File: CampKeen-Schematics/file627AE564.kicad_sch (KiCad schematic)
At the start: 25 parts, among them Q16 2N7000, Q17 2N7000, Q18 2N7000, Q19 2N7000, Q60 LTV-847

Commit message: working on input protection.
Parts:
- Q60: footprint DIP762W60P254L1984H450Q16N -> SamacSys_Parts:DIP762W60P254L1984H450Q16N
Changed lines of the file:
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@@
     (property "Reference" "Q60" (id 0) (at 158.75 64.389 0))
     (property "Value" "LTV-847" (id 1) (at 158.75 66.7004 0))
-    (property "Footprint" "DIP762W60P254L1984H450Q16N" (id 2) (at 176.53 68.58 0)
+    (property "Footprint" "SamacSys_Parts:DIP762W60P254L1984H450Q16N" (id 2) (at 176.53 68.58 0)
       (effects (font (size 1.27 1.27)) (justify left) hide)
     )

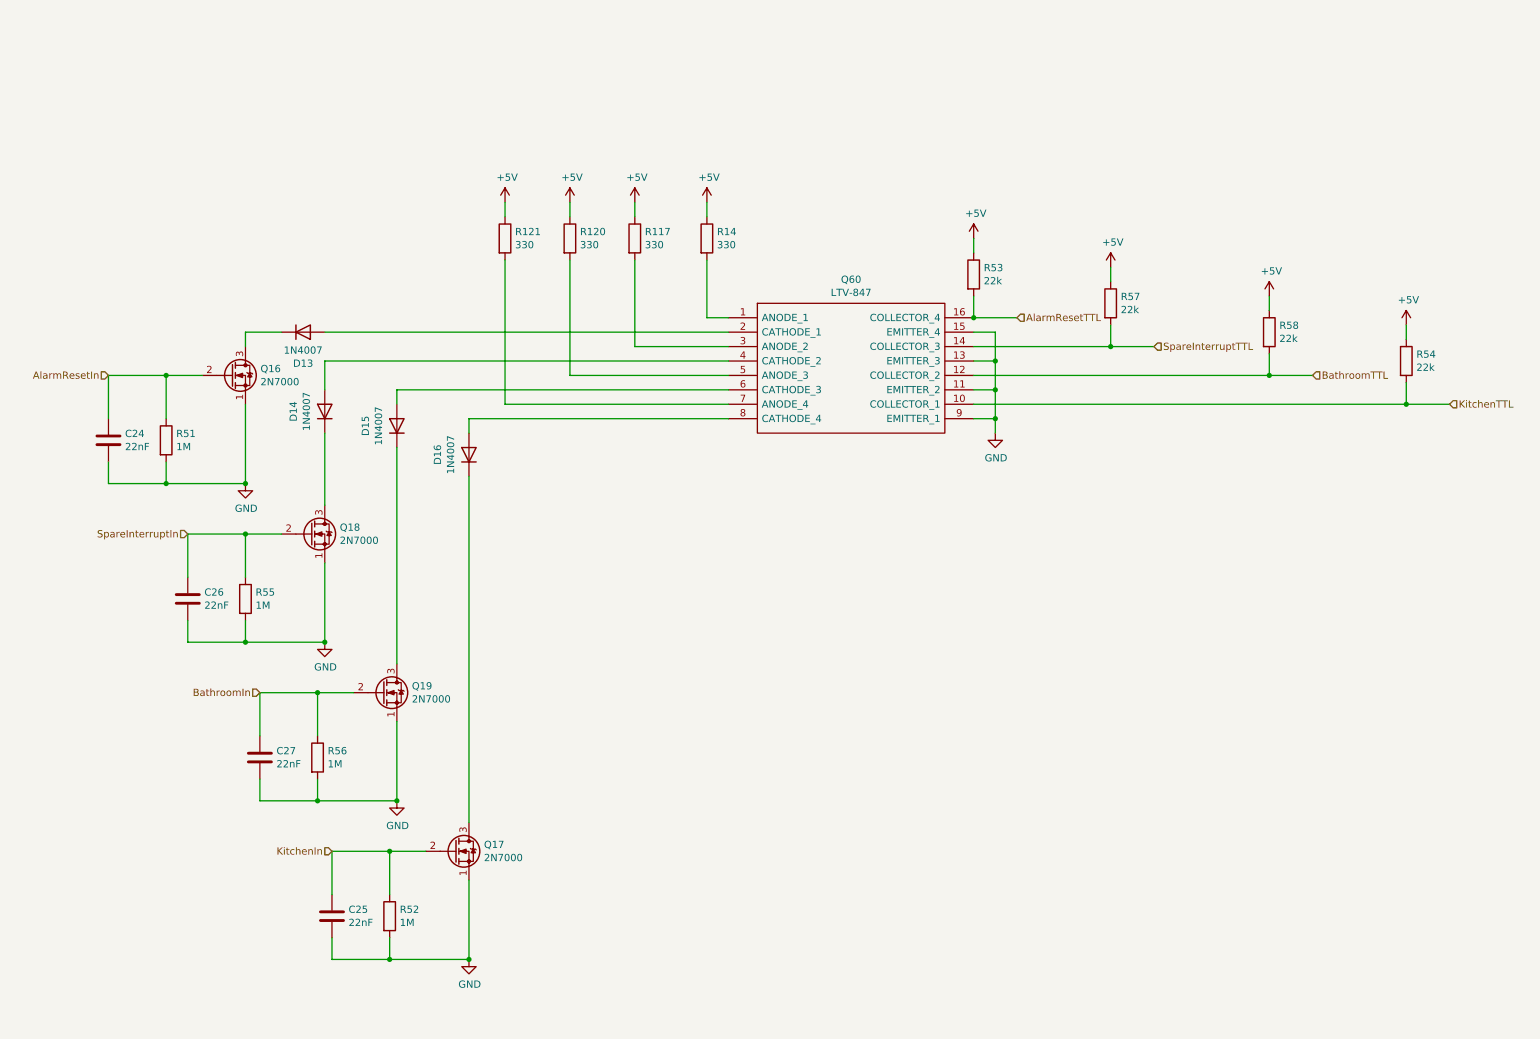
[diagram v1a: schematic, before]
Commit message: working on the input changes. removing all of the inverters. requires a code change. waiting on a part file to add the possible TVS diode
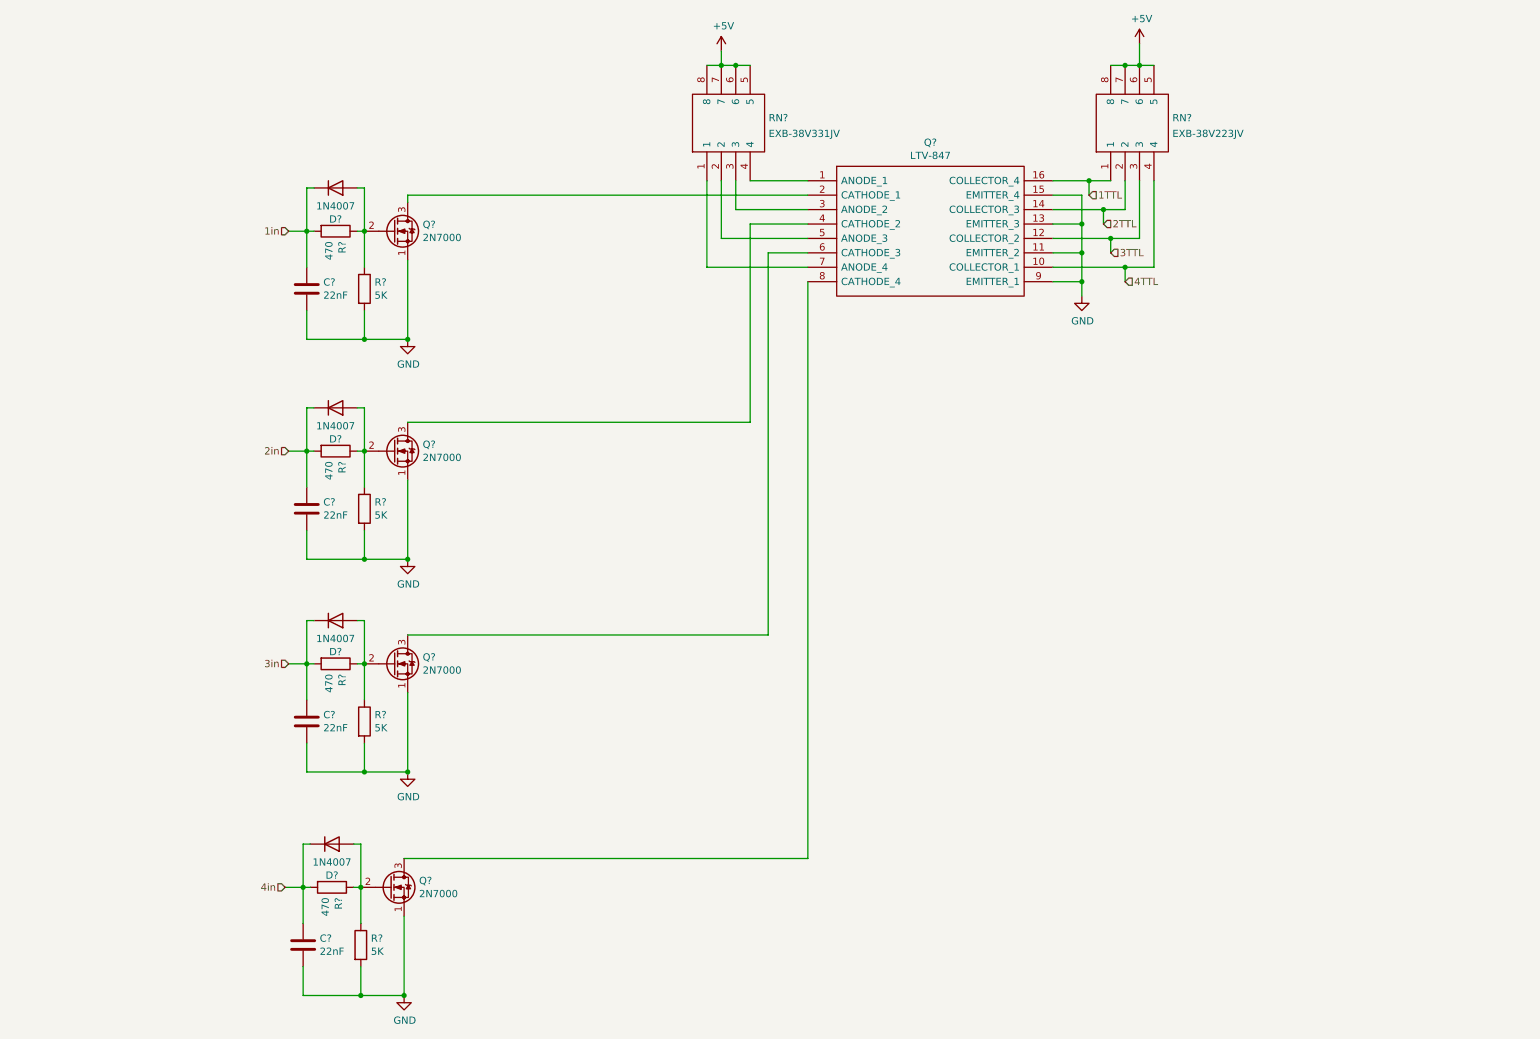
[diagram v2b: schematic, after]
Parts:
- removed C24, C25, C26, C27: 22nF, Capacitor_THT:C_Disc_D4.7mm_W2.5mm_P5.00mm, symbol Device:C
- removed D13, D14, D15, D16: 1N4007, Diode_THT:D_DO-41_SOD81_P10.16mm_Horizontal, symbol Diode:1N4007
- removed Q16, Q17, Q18, Q19: 2N7000, Package_TO_SOT_THT:TO-92_Inline, symbol Transistor_FET:2N7000
- removed Q60: LTV-847, SamacSys_Parts:DIP762W60P254L1984H450Q16N, symbol SamacSys_Parts:LTV-847
- removed R117, R120, R121, R14: 330, Resistor_THT:R_Axial_DIN0207_L6.3mm_D2.5mm_P2.54mm_Vertical, symbol Device:R
- removed R51, R52, R55, R56: 1M, Resistor_THT:R_Axial_DIN0207_L6.3mm_D2.5mm_P2.54mm_Vertical, symbol Device:R
- removed R53, R54, R57, R58: 22k, Resistor_THT:R_Axial_DIN0207_L6.3mm_D2.5mm_P2.54mm_Vertical, symbol Device:R
- added C? (x4): 22nF, Capacitor_SMD:C_0603_1608Metric_Pad1.08x0.95mm_HandSolder, symbol Device:C
- added D? (x4): 1N4007, Diode_THT:D_DO-41_SOD81_P10.16mm_Horizontal, symbol Diode:1N4007
- added Q? (x4): 2N7000, Package_TO_SOT_THT:TO-92_Inline, symbol Transistor_FET:2N7000
- added Q?: LTV-847, SamacSys_Parts:DIP762W60P254L1984H450Q16N, symbol SamacSys_Parts:LTV-847
- added R? (x4): 470, Resistor_THT:R_Axial_DIN0207_L6.3mm_D2.5mm_P2.54mm_Vertical, symbol Device:R
- added R? (x4): 5K, Resistor_THT:R_Axial_DIN0207_L6.3mm_D2.5mm_P2.54mm_Vertical, symbol Device:R
- added RN?: EXB-38V331JV, EXB38V472JV, symbol Samac_Sys:EXB-38V331JV
- added RN?: EXB-38V223JV, EXB38V472JV, symbol Samac_Sys:EXB-38V223JV
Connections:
- net +5V: now also RN?.5, RN?.5, RN?.6, RN?.6, RN?.7, RN?.7, RN?.8, RN?.8
- net GND: now also C?.2, C?.2, C?.2, C?.2, Q?.1 (S), Q?.1 (S), Q?.1 (S), Q?.1 (S), Q?.11 (EMITTER_2), Q?.13 (EMITTER_3), Q?.15 (EMITTER_4), Q?.9 (EMITTER_1), R?.2, R?.2, R?.2, R?.2
- new net: D?.2 (A), Q?.2 (G), R?.1, R?.1 (x4)
- new net: Q?.7 (ANODE_4), RN?.1
- new net: Q?.5 (ANODE_3), RN?.2
- new net: Q?.3 (ANODE_2), RN?.3
- new net: Q?.1 (ANODE_1), RN?.4
- new net: Q?.2 (CATHODE_1), Q?.3 (D)
- new net: Q?.3 (D), Q?.4 (CATHODE_2)
- new net: Q?.3 (D), Q?.6 (CATHODE_3)
- new net: Q?.3 (D), Q?.8 (CATHODE_4)
- new net 1TTL: Q?.16 (COLLECTOR_4), RN?.1
- new net 1in: C?.1, D?.1 (K), R?.2
- new net 2TTL: Q?.14 (COLLECTOR_3), RN?.2
- new net 2in: C?.1, D?.1 (K), R?.2
- new net 3TTL: Q?.12 (COLLECTOR_2), RN?.3
- new net 3in: C?.1, D?.1 (K), R?.2
- new net 4TTL: Q?.10 (COLLECTOR_1), RN?.4
- new net 4in: C?.1, D?.1 (K), R?.2

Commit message: wip
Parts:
- gave numbers to parts that had none: 23
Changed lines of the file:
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@@
   (symbol (lib_id "Device:R") (at 67.945 132.08 270)
     (in_bom yes) (on_board yes)
-    (property "Reference" "R?" (id 0) (at 69.1134 133.858 0)
+    (property "Reference" "R70" (id 0) (at 69.1134 133.858 0)
       (effects (font (size 1.27 1.27)) (justify left))
     )
@@
   (symbol (lib_id "Diode:1N4007") (at 67.945 86.995 0) (mirror x)
     (in_bom yes) (on_board yes)
-    (property "Reference" "D?" (id 0) (at 67.945 92.5068 0))
+    (property "Reference" "D22" (id 0) (at 67.945 92.5068 0))
     (property "Value" "1N4007" (id 1) (at 67.945 90.1954 0))
     (property "Footprint" "Diode_THT:D_DO-41_SOD81_P10.16mm_Horizontal" (id 2) (at 67.945 82.55 0)
@@
   (symbol (lib_id "power:+5V") (at 135.89 24.13 0)
     (in_bom yes) (on_board yes)
-    (property "Reference" "#PWR?" (id 0) (at 135.89 27.94 0)
+    (property "Reference" "#PWR0152" (id 0) (at 135.89 27.94 0)
       (effects (font (size 1.27 1.27)) hide)
     )
@@
   (symbol (lib_id "Samac_Sys:EXB-38V331JV") (at 133.35 46.99 90)
     (in_bom yes) (on_board yes) (fields_autoplaced)
-    (property "Reference" "RN?" (id 0) (at 144.2212 35.9215 90)
+    (property "Reference" "RN9" (id 0) (at 144.2212 35.9215 90)
       (effects (font (size 1.27 1.27)) (justify right))
     )
@@
   (symbol (lib_id "power:GND") (at 80.645 151.13 0)
     (in_bom yes) (on_board yes)
-    (property "Reference" "#PWR?" (id 0) (at 80.645 157.48 0)
+    (property "Reference" "#PWR0156" (id 0) (at 80.645 157.48 0)
       (effects (font (size 1.27 1.27)) hide)
     )
@@
   (symbol (lib_id "Transistor_FET:2N7000") (at 78.105 55.88 0)
     (in_bom yes) (on_board yes)
-    (property "Reference" "Q?" (id 0) (at 83.2866 54.7116 0)
+    (property "Reference" "Q27" (id 0) (at 83.2866 54.7116 0)
       (effects (font (size 1.27 1.27)) (justify left))
     )
@@
   (symbol (lib_id "Device:R") (at 67.945 55.88 270)
     (in_bom yes) (on_board yes)
-    (property "Reference" "R?" (id 0) (at 69.1134 57.658 0)
+    (property "Reference" "R68" (id 0) (at 69.1134 57.658 0)
       (effects (font (size 1.27 1.27)) (justify left))
     )
@@
   (symbol (lib_id "Diode:1N4007") (at 67.945 124.46 0) (mirror x)
     (in_bom yes) (on_board yes)
-    (property "Reference" "D?" (id 0) (at 67.945 129.9718 0))
+    (property "Reference" "D23" (id 0) (at 67.945 129.9718 0))
     (property "Value" "1N4007" (id 1) (at 67.945 127.6604 0))
     (property "Footprint" "Diode_THT:D_DO-41_SOD81_P10.16mm_Horizontal" (id 2) (at 67.945 120.015 0)
@@
   (symbol (lib_id "power:GND") (at 199.39 67.31 0)
     (in_bom yes) (on_board yes)
-    (property "Reference" "#PWR?" (id 0) (at 199.39 73.66 0)
+    (property "Reference" "#PWR0155" (id 0) (at 199.39 73.66 0)
       (effects (font (size 1.27 1.27)) hide)
     )
@@
   (symbol (lib_id "SamacSys_Parts:LTV-847") (at 151.13 46.99 0)
     (in_bom yes) (on_board yes)
-    (property "Reference" "Q?" (id 0) (at 172.72 40.259 0))
+    (property "Reference" "Q54" (id 0) (at 172.72 40.259 0))
     (property "Value" "LTV-847" (id 1) (at 172.72 42.5704 0))
     (property "Footprint" "SamacSys_Parts:DIP762W60P254L1984H450Q16N" (id 2) (at 190.5 44.45 0)
@@
   (symbol (lib_id "power:GND") (at 80.645 113.665 0)
     (in_bom yes) (on_board yes)
-    (property "Reference" "#PWR?" (id 0) (at 80.645 120.015 0)
+    (property "Reference" "#PWR0123" (id 0) (at 80.645 120.015 0)
       (effects (font (size 1.27 1.27)) hide)
     )
@@
   (symbol (lib_id "power:GND") (at 80.01 190.5 0)
     (in_bom yes) (on_board yes)
-    (property "Reference" "#PWR?" (id 0) (at 80.01 196.85 0)
+    (property "Reference" "#PWR0150" (id 0) (at 80.01 196.85 0)
       (effects (font (size 1.27 1.27)) hide)
     )
@@
   (symbol (lib_id "Device:R") (at 67.945 94.615 270)
     (in_bom yes) (on_board yes)
-    (property "Reference" "R?" (id 0) (at 69.1134 96.393 0)
+    (property "Reference" "R69" (id 0) (at 69.1134 96.393 0)
       (effects (font (size 1.27 1.27)) (justify left))
     )
@@
   (symbol (lib_id "Diode:1N4007") (at 67.31 163.83 0) (mirror x)
     (in_bom yes) (on_board yes)
-    (property "Reference" "D?" (id 0) (at 67.31 169.3418 0))
+    (property "Reference" "D20" (id 0) (at 67.31 169.3418 0))
     (property "Value" "1N4007" (id 1) (at 67.31 167.0304 0))
     (property "Footprint" "Diode_THT:D_DO-41_SOD81_P10.16mm_Horizontal" (id 2) (at 67.31 159.385 0)
@@
   (symbol (lib_id "Device:R") (at 67.31 171.45 270)
     (in_bom yes) (on_board yes)
-    (property "Reference" "R?" (id 0) (at 68.4784 173.228 0)
+    (property "Reference" "R67" (id 0) (at 68.4784 173.228 0)
       (effects (font (size 1.27 1.27)) (justify left))
     )
@@
   (symbol (lib_id "Device:R") (at 73.025 104.775 0)
     (in_bom yes) (on_board yes)
-    (property "Reference" "R?" (id 0) (at 74.803 103.6066 0)
+    (property "Reference" "R73" (id 0) (at 74.803 103.6066 0)
       (effects (font (size 1.27 1.27)) (justify left))
     )
@@
   (symbol (lib_id "Device:R") (at 73.025 142.24 0)
     (in_bom yes) (on_board yes)
-    (property "Reference" "R?" (id 0) (at 74.803 141.0716 0)
+    (property "Reference" "R74" (id 0) (at 74.803 141.0716 0)
       (effects (font (size 1.27 1.27)) (justify left))
     )
@@
   (symbol (lib_id "Transistor_FET:2N7000") (at 77.47 171.45 0)
     (in_bom yes) (on_board yes)
-    (property "Reference" "Q?" (id 0) (at 82.6516 170.2816 0)
+    (property "Reference" "Q26" (id 0) (at 82.6516 170.2816 0)
       (effects (font (size 1.27 1.27)) (justify left))
     )
@@
   (symbol (lib_id "Device:C") (at 62.865 66.04 0)
     (in_bom yes) (on_board yes)
-    (property "Reference" "C?" (id 0) (at 65.786 64.8716 0)
+    (property "Reference" "C38" (id 0) (at 65.786 64.8716 0)
       (effects (font (size 1.27 1.27)) (justify left))
     )
@@
   (symbol (lib_id "power:GND") (at 80.645 74.93 0)
     (in_bom yes) (on_board yes)
-    (property "Reference" "#PWR?" (id 0) (at 80.645 81.28 0)
+    (property "Reference" "#PWR0124" (id 0) (at 80.645 81.28 0)
       (effects (font (size 1.27 1.27)) hide)
     )
@@
   (symbol (lib_id "Device:R") (at 73.025 66.04 0)
     (in_bom yes) (on_board yes)
-    (property "Reference" "R?" (id 0) (at 74.803 64.8716 0)
+    (property "Reference" "R72" (id 0) (at 74.803 64.8716 0)
       (effects (font (size 1.27 1.27)) (justify left))
     )
@@
   (symbol (lib_id "Device:R") (at 72.39 181.61 0)
     (in_bom yes) (on_board yes)
-    (property "Reference" "R?" (id 0) (at 74.168 180.4416 0)
+    (property "Reference" "R71" (id 0) (at 74.168 180.4416 0)
       (effects (font (size 1.27 1.27)) (justify left))
     )
@@
   (symbol (lib_id "Transistor_FET:2N7000") (at 78.105 132.08 0)
     (in_bom yes) (on_board yes)
-    (property "Reference" "Q?" (id 0) (at 83.2866 130.9116 0)
+    (property "Reference" "Q29" (id 0) (at 83.2866 130.9116 0)
       (effects (font (size 1.27 1.27)) (justify left))
     )
@@
   (symbol (lib_id "Device:C") (at 62.865 104.775 0)
     (in_bom yes) (on_board yes)
-    (property "Reference" "C?" (id 0) (at 65.786 103.6066 0)
+    (property "Reference" "C39" (id 0) (at 65.786 103.6066 0)
       (effects (font (size 1.27 1.27)) (justify left))
     )
@@
   (symbol (lib_id "power:+5V") (at 209.55 22.86 0)
     (in_bom yes) (on_board yes)
-    (property "Reference" "#PWR?" (id 0) (at 209.55 26.67 0)
+    (property "Reference" "#PWR0153" (id 0) (at 209.55 26.67 0)
       (effects (font (size 1.27 1.27)) hide)
     )
@@
   (symbol (lib_id "Samac_Sys:EXB-38V223JV") (at 204.47 46.99 90)
     (in_bom yes) (on_board yes) (fields_autoplaced)
-    (property "Reference" "RN?" (id 0) (at 215.3412 35.9215 90)
+    (property "Reference" "RN10" (id 0) (at 215.3412 35.9215 90)
       (effects (font (size 1.27 1.27)) (justify right))
     )
@@
   (symbol (lib_id "Transistor_FET:2N7000") (at 78.105 94.615 0)
     (in_bom yes) (on_board yes)
-    (property "Reference" "Q?" (id 0) (at 83.2866 93.4466 0)
+    (property "Reference" "Q28" (id 0) (at 83.2866 93.4466 0)
       (effects (font (size 1.27 1.27)) (justify left))
     )
@@
   (symbol (lib_id "Device:C") (at 62.23 181.61 0)
     (in_bom yes) (on_board yes)
-    (property "Reference" "C?" (id 0) (at 65.151 180.4416 0)
+    (property "Reference" "C37" (id 0) (at 65.151 180.4416 0)
       (effects (font (size 1.27 1.27)) (justify left))
     )
@@
   (symbol (lib_id "Device:C") (at 62.865 142.24 0)
     (in_bom yes) (on_board yes)
-    (property "Reference" "C?" (id 0) (at 65.786 141.0716 0)
+    (property "Reference" "C40" (id 0) (at 65.786 141.0716 0)
       (effects (font (size 1.27 1.27)) (justify left))
     )
@@
   (symbol (lib_id "Diode:1N4007") (at 67.945 48.26 0) (mirror x)
     (in_bom yes) (on_board yes)
-    (property "Reference" "D?" (id 0) (at 67.945 53.7718 0))
+    (property "Reference" "D21" (id 0) (at 67.945 53.7718 0))
     (property "Value" "1N4007" (id 1) (at 67.945 51.4604 0))
     (property "Footprint" "Diode_THT:D_DO-41_SOD81_P10.16mm_Horizontal" (id 2) (at 67.945 43.815 0)
